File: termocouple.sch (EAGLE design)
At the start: 22 parts, among them IC1 MAX6675, IC2 MAX6675, IC3 MAX6675, IC4 MAX6675, U2 TC1262_VDB, X2 1751248, X3 1751248, X4 1751248, X5 1751248

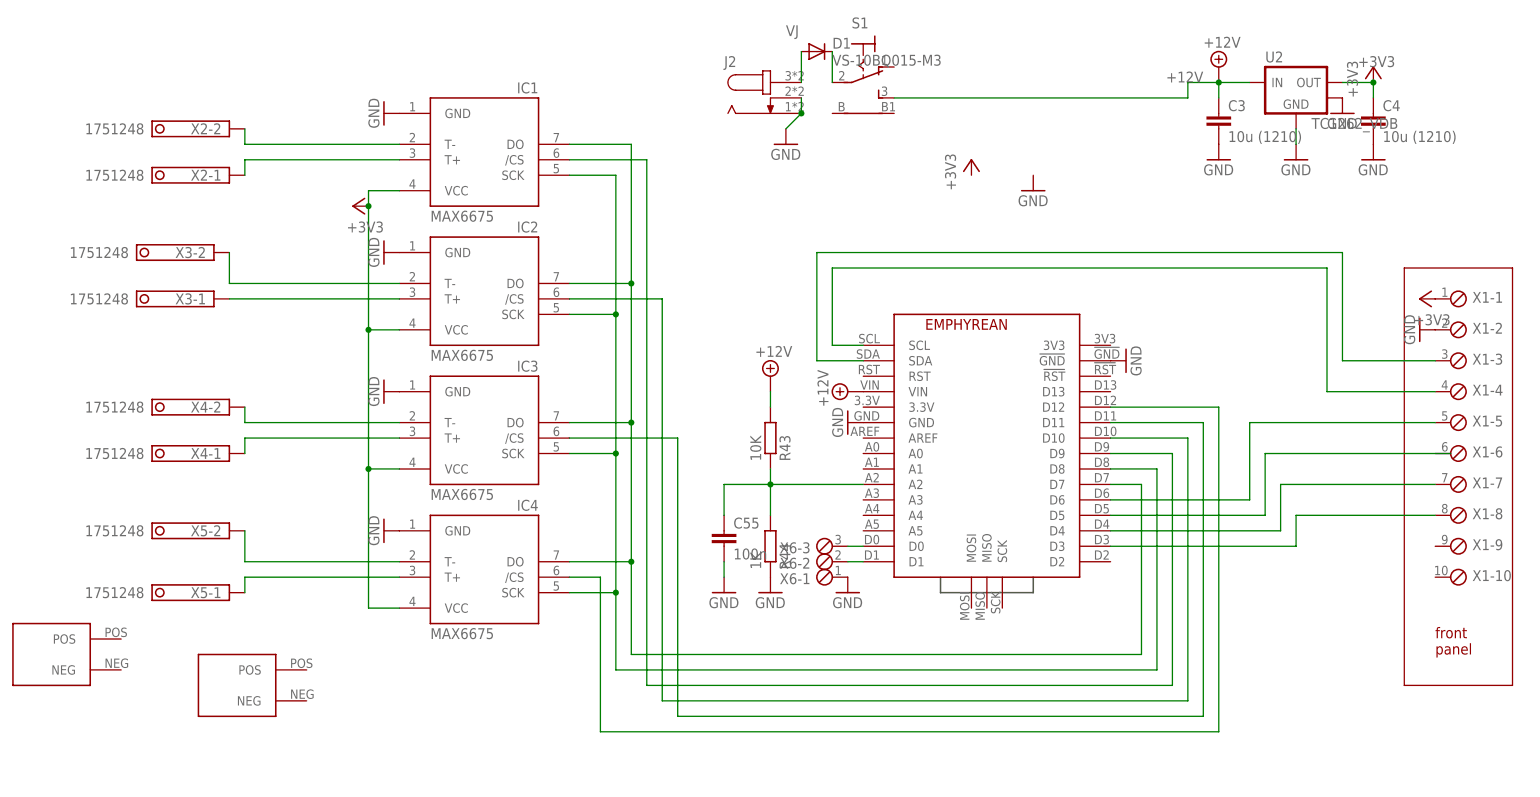
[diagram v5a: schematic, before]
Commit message: readme update, arm definitions, pcb moved to 2 sensor
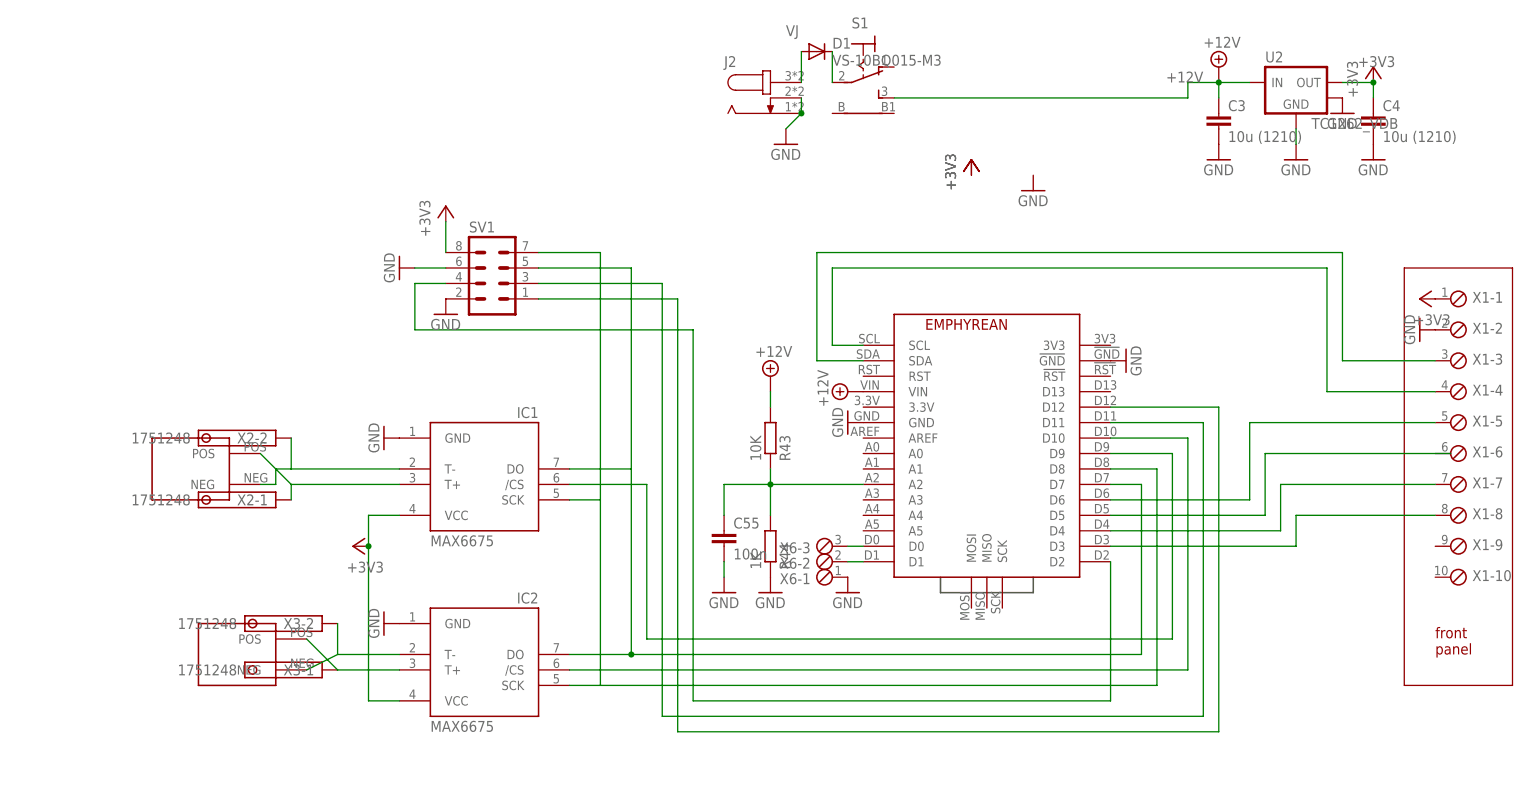
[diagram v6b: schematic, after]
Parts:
- removed IC3, IC4: MAX6675, adafruit:MAX6675
- removed X4, X5: 1751248, con-phoenix-350:1751248
- added SV1: (no value), con-lstb:MA04-2
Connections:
- removed net N$16: IC3.T-, X4-2.K
- removed net N$17: IC3.T+, X4-1.K
- removed net N$6: IC3./CS, U$1.D11
- net +3V3: now also SV1.8; no longer IC3.VCC, IC4.VCC
- net GND: now also SV1.2, SV1.6; no longer IC3.GND, IC4.GND
- net N$1: now also SV1.5; no longer IC3.DO, IC4.DO
- net N$14: now also SV1.1, U$1.D12; no longer IC4.T+, X5-1.K
- net N$15: now also SV1.4, U$1.D2; no longer IC4.T-, X5-2.K
- net N$18: now also U$2.POS
- net N$19: now also U$2.NEG
- net N$2: now also SV1.7; no longer IC3.SCK, IC4.SCK
- net N$20: now also U$3.POS
- net N$21: now also U$3.NEG
- net N$7: now also SV1.3, U$1.D11; no longer IC4./CS, U$1.D12
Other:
- moved on the sheet: IC1, IC2, X2-1, X2-2, X3-1, X3-2

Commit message: pdf version of schematics
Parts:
- IC1, IC2: value MAX6675 -> MAX31855
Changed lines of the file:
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@@
 <parts>
 <part name="U$1" library="mine" deviceset="EPHYREAN" device=""/>
-<part name="IC1" library="adafruit" deviceset="MAX6675" device=""/>
-<part name="IC2" library="adafruit" deviceset="MAX6675" device=""/>
+<part name="IC1" library="adafruit" deviceset="MAX6675" device="" value="MAX31855"/>
+<part name="IC2" library="adafruit" deviceset="MAX6675" device="" value="MAX31855"/>
 <part name="+3V1" library="supply1" deviceset="+3V3" device=""/>
 <part name="GND1" library="supply1" deviceset="GND" device=""/>

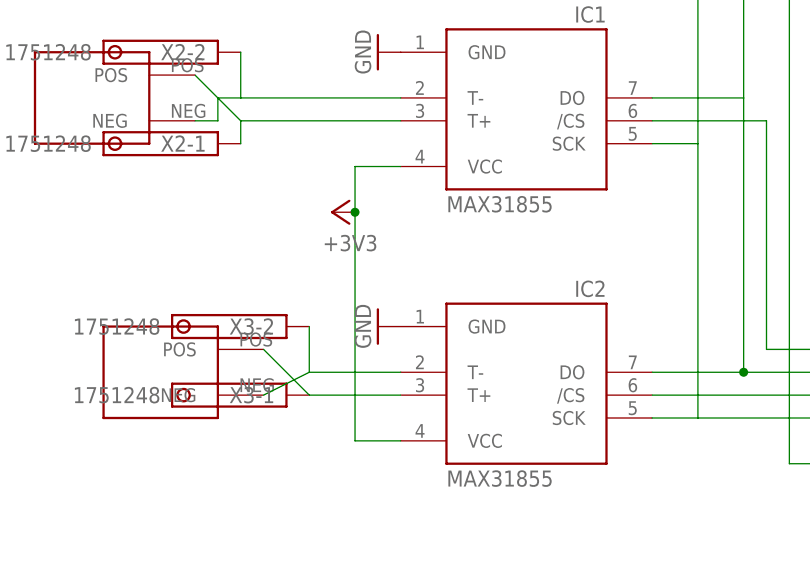
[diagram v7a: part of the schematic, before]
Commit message: pcb fix
Fix PCB's to make it possible to build the boards without rework
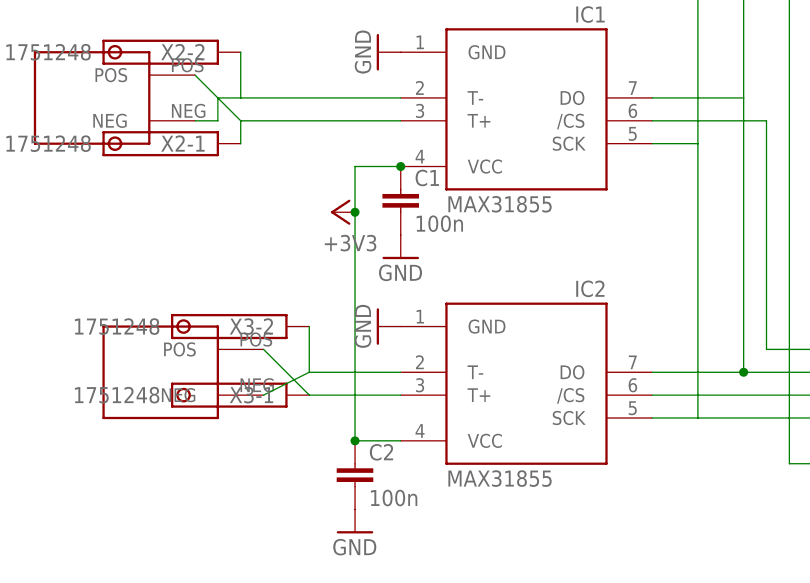
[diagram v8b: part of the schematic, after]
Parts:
- added C1, C2: 100n, rcl:C-EUC1206
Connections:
- net +3V3: now also C1.1, C2.1
- net GND: now also C1.2, C2.2
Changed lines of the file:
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@@
 <part name="+3V2" library="supply1" deviceset="+3V3" device=""/>
 <part name="+3V3" library="supply1" deviceset="+3V3" device=""/>
+<part name="C1" library="rcl" deviceset="C-EU" device="C1206" value="100n"/>
+<part name="C2" library="rcl" deviceset="C-EU" device="C1206" value="100n"/>
+<part name="GND15" library="supply1" deviceset="GND" device=""/>
+<part name="GND16" library="supply1" deviceset="GND" device=""/>
 </parts>
 <sheets>
@@
 <instance part="+3V2" gate="G$1" x="76.2" y="86.36"/>
 <instance part="+3V3" gate="G$1" x="-10.16" y="78.74"/>
+<instance part="C1" gate="G$1" x="-17.78" y="25.4"/>
+<instance part="C2" gate="G$1" x="-22.86" y="-5.08"/>
+<instance part="GND15" gate="1" x="-17.78" y="17.78"/>
+<instance part="GND16" gate="1" x="-22.86" y="-12.7"/>
 </instances>
 <busses>
@@
 <pinref part="+3V1" gate="G$1" pin="+3V3"/>
 <junction x="-22.86" y="22.86"/>
+<pinref part="C1" gate="G$1" pin="1"/>
+<junction x="-17.78" y="27.94"/>
+<pinref part="C2" gate="G$1" pin="1"/>
+<junction x="-22.86" y="-2.54"/>
 </segment>
 <segment>
@@
 <wire x1="-15.24" y1="68.58" x2="-10.16" y2="68.58" width="0.1524" layer="91"/>
 </segment>
-</net>
+<segment>
+<pinref part="C1" gate="G$1" pin="2"/>
+<pinref part="GND15" gate="1" pin="GND"/>
+</segment>
+<segment>
+<pinref part="C2" gate="G$1" pin="2"/>
+<pinref part="GND16" gate="1" pin="GND"/>
+</segment>
+</net>
